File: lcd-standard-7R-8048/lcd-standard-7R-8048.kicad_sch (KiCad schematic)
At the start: 109 parts, among them J1 SWD, J10 Conn_01x10_MountingPin, J2 Conn_01x40_MountingPin, J3 Micro_SD_Card_Det1, J6 Serial, J7 Conn_ARM_JTAG_SWD_10, J8 Conn_01x02_MountingPin, J9 Conn_01x10_MountingPin, Q1 DMG2301L, Q2 MMBT3904, Q3 MMBT3904, Q4 MMBT3904, SW1 BOOT0, SW2 RST, U1 MAX98357A, U2 TPS61169, U3 XPT2046TS, U4 CAT24C256, U5 AMS1117-3.3, U6 siplex-som-s16

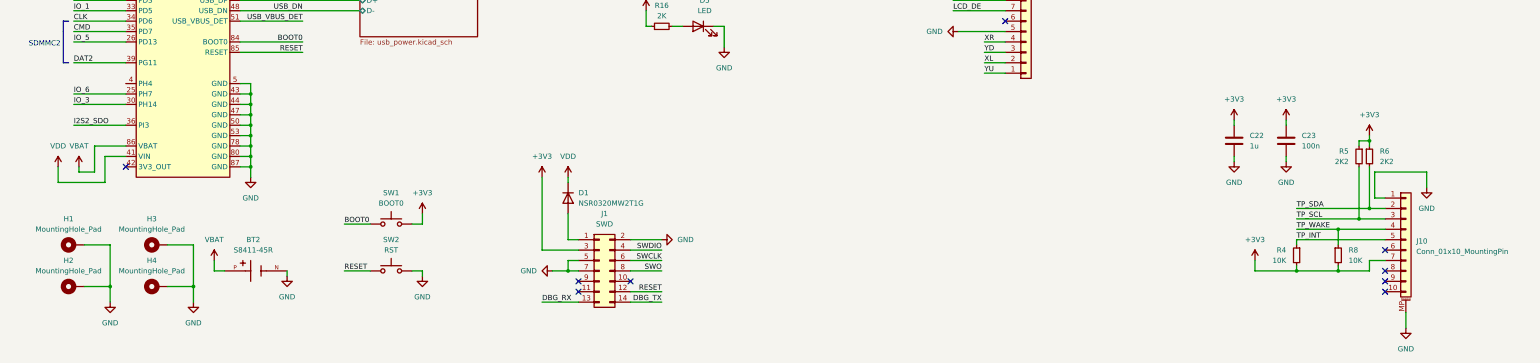
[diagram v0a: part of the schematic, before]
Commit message: Layouting LCD 7R, LED's and PWR tracks left
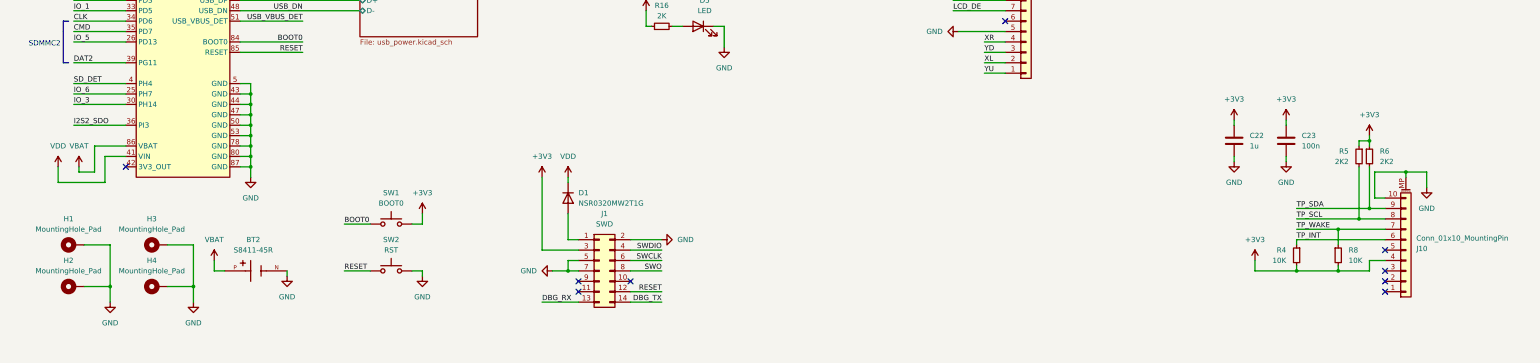
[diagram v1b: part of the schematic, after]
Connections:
- net +3V3: now also J10.4 (Pin_4); no longer J10.7 (Pin_7)
- net GND: now also J10.10 (Pin_10); no longer J10.1 (Pin_1)
- net SD_DET: now also U6.4 (PH4)
- net TP_INT: now also J10.6 (Pin_6); no longer J10.5 (Pin_5)
- net TP_SCL: now also J10.8 (Pin_8); no longer J10.3 (Pin_3)
- net TP_SDA: now also J10.9 (Pin_9); no longer J10.2 (Pin_2)
- net TP_WAKE: now also J10.7 (Pin_7); no longer J10.4 (Pin_4)
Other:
- moved on the sheet: J10
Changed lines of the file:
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@@
 	)
 	(junction
+		(at 349.25 160.02)
+		(diameter 0)
+		(color 0 0 0 0)
+	)
+	(junction
 		(at 67.31 140.97)
 		(diameter 0)
@@
 	(wire
 		(pts
-			(xy 349.25 194.31) (xy 349.25 198.12)
-		)
-		(stroke
-			(width 0)
-			(type default)
-		)
-	)
-	(wire
-		(pts
 			(xy 172.72 85.09) (xy 196.85 85.09)
 		)
@@
 	(wire
 		(pts
+			(xy 349.25 160.02) (xy 341.63 160.02)
+		)
+		(stroke
+			(width 0)
+			(type default)
+		)
+	)
+	(wire
+		(pts
 			(xy -40.64 44.45) (xy -50.8 44.45)
 		)
@@
 	(wire
 		(pts
+			(xy 349.25 160.02) (xy 349.25 161.29)
+		)
+		(stroke
+			(width 0)
+			(type default)
+		)
+	)
+	(wire
+		(pts
 			(xy 173.99 30.48) (xy 163.83 30.48)
 		)
@@
 	(wire
 		(pts
+			(xy 24.13 138.43) (xy 36.83 138.43)
+		)
+		(stroke
+			(width 0)
+			(type default)
+		)
+	)
+	(wire
+		(pts
 			(xy 82.55 -11.43) (xy 82.55 -13.97)
 		)
@@
 	(wire
 		(pts
-			(xy 354.33 160.02) (xy 341.63 160.02)
+			(xy 354.33 160.02) (xy 349.25 160.02)
 		)
 		(stroke
@@
 		)
 	)
+	(label "SD_DET"
+		(at 24.13 138.43 0)
+		(fields_autoplaced yes)
+		(effects
+			(font
+				(size 1.27 1.27)
+			)
+			(justify left bottom)
+		)
+	)
 	(label "USB_VBUS_DET"
 		(at 80.01 123.19 180)
@@
 	(symbol
 		(lib_id "Connector_Generic_MountingPin:Conn_01x10_MountingPin")
-		(at 349.25 176.53 0)
+		(at 349.25 179.07 0)
+		(mirror x)
 		(unit 1)
 		(exclude_from_sim no)
@@
 		(on_board yes)
 		(dnp no)
-		(fields_autoplaced yes)
 		(property "Reference" "J10"
-			(at 351.79 176.8855 0)
+			(at 351.79 178.7145 0)
 			(effects
 				(font
@@
 		)
 		(property "Value" "Conn_01x10_MountingPin"
-			(at 351.79 179.4255 0)
+			(at 351.79 176.1745 0)
 			(effects
 				(font
@@
 		)
 		(property "Footprint" "Connector_FFC-FPC:Hirose_FH12-10S-0.5SH_1x10-1MP_P0.50mm_Horizontal"
-			(at 349.25 176.53 0)
+			(at 349.25 179.07 0)
 			(effects
 				(font
@@
 		)
 		(property "Datasheet" "~"
-			(at 349.25 176.53 0)
+			(at 349.25 179.07 0)
 			(effects
 				(font
@@
 		)
 		(property "Description" "Generic connectable mounting pin connector, single row, 01x10, script generated (kicad-library-utils/schlib/autogen/connector/)"
-			(at 349.25 176.53 0)
+			(at 349.25 179.07 0)
 			(effects
 				(font
@@
 					(unit 1)
 				)
-			)
-		)
-	)
-	(symbol
-		(lib_id "power:GND")
-		(at 349.25 198.12 0)
-		(unit 1)
-		(exclude_from_sim no)
-		(in_bom yes)
-		(on_board yes)
-		(dnp no)
-		(fields_autoplaced yes)
-		(property "Reference" "#PWR0107"
-			(at 349.25 204.47 0)
-			(effects
-				(font
-					(size 1.27 1.27)
-				)
-				(hide yes)
-			)
-		)
-		(property "Value" "GND"
-			(at 349.25 203.2 0)
-			(effects
-				(font
-					(size 1.27 1.27)
-				)
-			)
-		)
-		(property "Footprint" ""
-			(at 349.25 198.12 0)
-			(effects
-				(font
-					(size 1.27 1.27)
-				)
-				(hide yes)
-			)
-		)
-		(property "Datasheet" ""
-			(at 349.25 198.12 0)
-			(effects
-				(font
-					(size 1.27 1.27)
-				)
-				(hide yes)
-			)
-		)
-		(property "Description" "Power symbol creates a global label with name \"GND\" , ground"
-			(at 349.25 198.12 0)
-			(effects
-				(font
-					(size 1.27 1.27)
-				)
-				(hide yes)
-			)
-		)
-		(pin "1"
-		)
-		(instances
-			(project "lcd-standard-7R-8048"
-				(path "/a9fe5be7-3a80-455e-a721-d53819db4a52"
-					(reference "#PWR0107")
-					(unit 1)
-				)
